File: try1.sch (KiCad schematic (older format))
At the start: 27 parts, among them J10 Archon-connector-modules-Driv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, J11 Archon-connector-modules-Driv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, J2 Archon-connector-modules-Heat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, J21 DB37, J22 DB37, J3 Archon-connector-modules-Driv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, J31 DB9, J4 Archon-connector-modules-LVBi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, J41 CONN_DVI, J5 Archon-connector-modules-ADC, J6 Archon-connector-modules-ADC, J7 Archon-connector-modules-ADC, J8 Archon-connector-modules-ADC, J9 Archon-connector-modules-HVBi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

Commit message: Auto-Annotate
Annotate parts added since the last time I did it.
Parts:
- gave numbers to parts that had none: 13
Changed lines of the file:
@@
 HV9_10
 $Comp
-L CONN_02X02 P?
+L CONN_02X02 P1
 U 1 1 57B547B3
 P 20850 4650
-F 0 "P?" H 20850 4800 50  0000 C CNN
+F 0 "P1" H 20850 4800 50  0000 C CNN
 F 1 "CONN_02X02" H 20850 4500 50  0000 C CNN
 F 2 "ccdcamera:Molex_MiniFit-JR-5556-04B_2x02x4.20mm_Straight" H 20850 3450 50  0000 C CNN
@@
 HEATER1_TEMPB_SP
 $Comp
-L TEST_1P W?
+L TEST_1P W5
 U 1 1 57B5D36F
 P 22650 2500
-F 0 "W?" H 22650 2770 50  0000 C CNN
+F 0 "W5" H 22650 2770 50  0000 C CNN
 F 1 "TEST_1P" H 22650 2700 50  0000 C CNN
 F 2 "" H 22850 2500 50  0000 C CNN
@@
 $EndComp
 $Comp
-L TEST_1P W?
+L TEST_1P W6
 U 1 1 57B5D617
 P 22950 2500
-F 0 "W?" H 22950 2770 50  0000 C CNN
+F 0 "W6" H 22950 2770 50  0000 C CNN
 F 1 "TEST_1P" H 22950 2700 50  0000 C CNN
 F 2 "" H 23150 2500 50  0000 C CNN
@@
 $EndComp
 $Comp
-L TEST_1P W?
+L TEST_1P W7
 U 1 1 57B5D666
 P 23250 2500
-F 0 "W?" H 23250 2770 50  0000 C CNN
+F 0 "W7" H 23250 2770 50  0000 C CNN
 F 1 "TEST_1P" H 23250 2700 50  0000 C CNN
 F 2 "" H 23450 2500 50  0000 C CNN
@@
 $EndComp
 $Comp
-L TEST_1P W?
+L TEST_1P W8
 U 1 1 57B5D69D
 P 23550 2500
-F 0 "W?" H 23550 2770 50  0000 C CNN
+F 0 "W8" H 23550 2770 50  0000 C CNN
 F 1 "TEST_1P" H 23550 2700 50  0000 C CNN
 F 2 "" H 23750 2500 50  0000 C CNN
@@
 $EndComp
 $Comp
-L TEST_1P W?
+L TEST_1P W9
 U 1 1 57B5D6ED
 P 23850 2500
-F 0 "W?" H 23850 2770 50  0000 C CNN
+F 0 "W9" H 23850 2770 50  0000 C CNN
 F 1 "TEST_1P" H 23850 2700 50  0000 C CNN
 F 2 "" H 24050 2500 50  0000 C CNN
@@
 $EndComp
 $Comp
-L TEST_1P W?
+L TEST_1P W10
 U 1 1 57B5D728
 P 24150 2500
-F 0 "W?" H 24150 2770 50  0000 C CNN
+F 0 "W10" H 24150 2770 50  0000 C CNN
 F 1 "TEST_1P" H 24150 2700 50  0000 C CNN
 F 2 "" H 24350 2500 50  0000 C CNN
@@
 LV4_5
 $Comp
-L TEST_1P W?
+L TEST_1P W1
 U 1 1 57BED8F1
 P 12150 7800
-F 0 "W?" H 12150 8070 50  0000 C CNN
+F 0 "W1" H 12150 8070 50  0000 C CNN
 F 1 "Spare1" H 12150 8000 50  0000 C CNN
 F 2 "" H 12350 7800 50  0000 C CNN
@@
 $EndComp
 $Comp
-L TEST_1P W?
+L TEST_1P W2
 U 1 1 57BEF217
 P 12450 7800
-F 0 "W?" H 12450 8070 50  0000 C CNN
+F 0 "W2" H 12450 8070 50  0000 C CNN
 F 1 "Spare4" H 12450 8000 50  0000 C CNN
 F 2 "" H 12650 7800 50  0000 C CNN
@@
 $EndComp
 $Comp
-L TEST_1P W?
+L TEST_1P W4
 U 1 1 57BEF28B
 P 15950 7800
-F 0 "W?" H 15950 8070 50  0000 C CNN
+F 0 "W4" H 15950 8070 50  0000 C CNN
 F 1 "Spare3" H 15950 8000 50  0000 C CNN
 F 2 "" H 16150 7800 50  0000 C CNN
@@
 $EndComp
 $Comp
-L TEST_1P W?
+L TEST_1P W3
 U 1 1 57BEF46D
 P 15600 7800
-F 0 "W?" H 15600 8070 50  0000 C CNN
+F 0 "W3" H 15600 8070 50  0000 C CNN
 F 1 "Spare2" H 15600 8000 50  0000 C CNN
 F 2 "" H 15800 7800 50  0000 C CNN
@@
 Spare_3
 $Comp
-L GND #PWR?
+L GND #PWR1
 U 1 1 57BF0379
 P 29050 3950
-F 0 "#PWR?" H 29050 3700 50  0001 C CNN
+F 0 "#PWR1" H 29050 3700 50  0001 C CNN
 F 1 "GND" H 29050 3800 50  0000 C CNN
 F 2 "" H 29050 3950 50  0000 C CNN
@@
 DRV3_GND
 $Comp
-L JUMPER JP?
+L JUMPER JP1
 U 1 1 57BF7B2C
 P 5950 4000
-F 0 "JP?" H 5950 4150 50  0000 C CNN
+F 0 "JP1" H 5950 4150 50  0000 C CNN
 F 1 "JUMPER" H 5950 3920 50  0000 C CNN
 F 2 "" H 5950 4000 50  0000 C CNN
@@
 $EndComp
 $Comp
-L JUMPER JP?
+L JUMPER JP2
 U 1 1 57BF7BA1
 P 5950 4300
-F 0 "JP?" H 5950 4450 50  0000 C CNN
+F 0 "JP2" H 5950 4450 50  0000 C CNN
 F 1 "JUMPER" H 5950 4220 50  0000 C CNN
 F 2 "" H 5950 4300 50  0000 C CNN

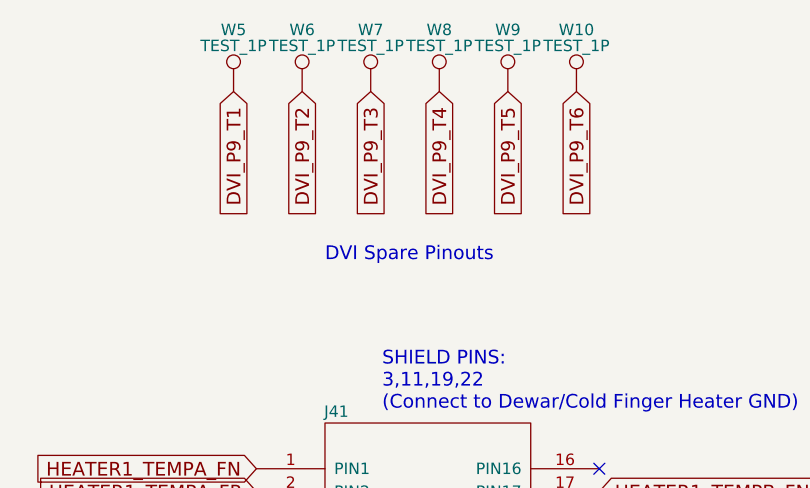
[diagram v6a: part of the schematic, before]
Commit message: Fix DVI spare pin label names
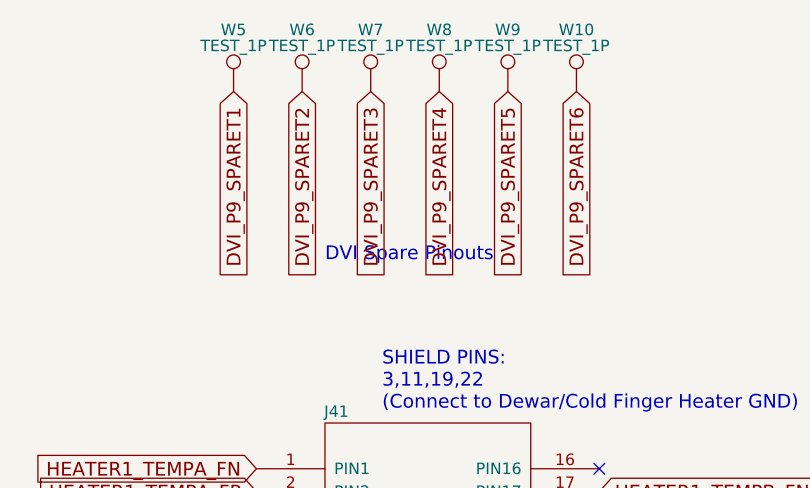
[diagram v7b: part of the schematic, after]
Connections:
- net labels removed: DVI_P9_T1, DVI_P9_T2, DVI_P9_T3, DVI_P9_T4, DVI_P9_T5, DVI_P9_T6
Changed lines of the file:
@@
 DVI_P9_SPARET6
 Text GLabel 22650 2500 3    60   Input ~ 0
-DVI_P9_T1
+DVI_P9_SPARET1
 Text GLabel 22950 2500 3    60   Input ~ 0
-DVI_P9_T2
+DVI_P9_SPARET2
 Text GLabel 23250 2500 3    60   Input ~ 0
-DVI_P9_T3
+DVI_P9_SPARET3
 Text GLabel 23550 2500 3    60   Input ~ 0
-DVI_P9_T4
+DVI_P9_SPARET4
 Text GLabel 23850 2500 3    60   Input ~ 0
-DVI_P9_T5
+DVI_P9_SPARET5
 Text GLabel 24150 2500 3    60   Input ~ 0
-DVI_P9_T6
+DVI_P9_SPARET6
 Text Notes 23300 3900 0    60   ~ 0
 SHIELD PINS:\n3,11,19,22\n(Connect to Dewar/Cold Finger Heater GND)
@@
 Spare_3
 $Comp
-L GND #PWR1
+L GND #PWR01
 U 1 1 57BF0379
 P 29050 3950
-F 0 "#PWR1" H 29050 3700 50  0001 C CNN
+F 0 "#PWR01" H 29050 3700 50  0001 C CNN
 F 1 "GND" H 29050 3800 50  0000 C CNN
 F 2 "" H 29050 3950 50  0000 C CNN
